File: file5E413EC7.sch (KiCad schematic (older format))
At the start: 4 parts

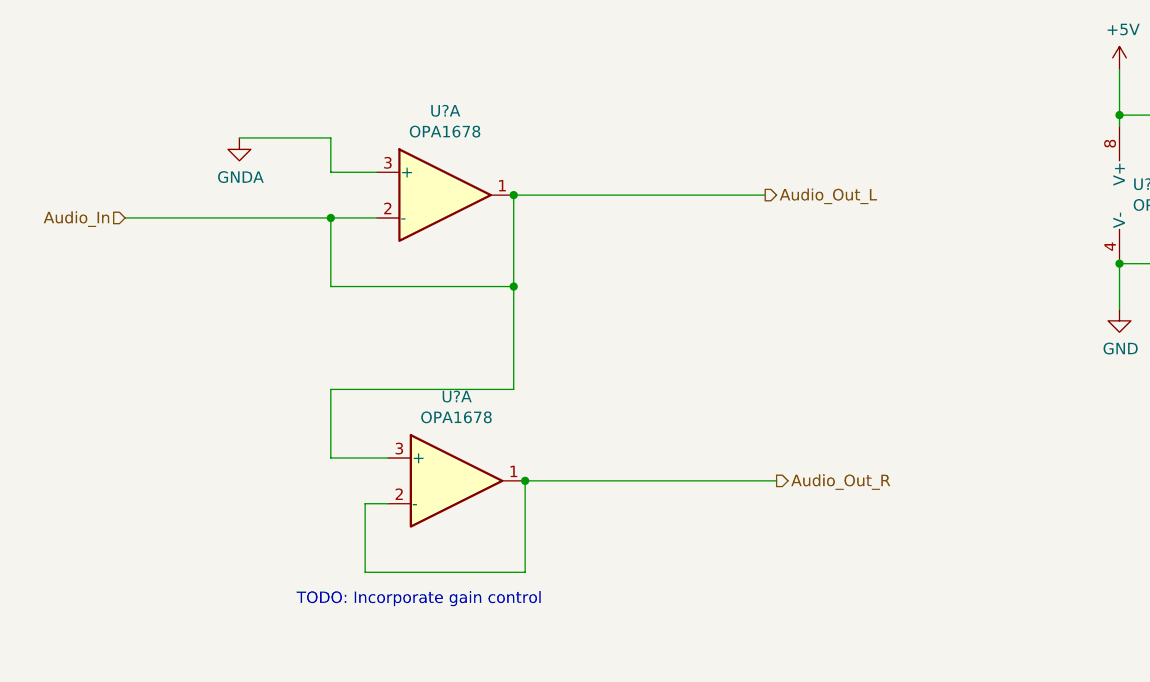
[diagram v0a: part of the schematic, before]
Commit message: Filter calculations, gain stage, oscillation protection
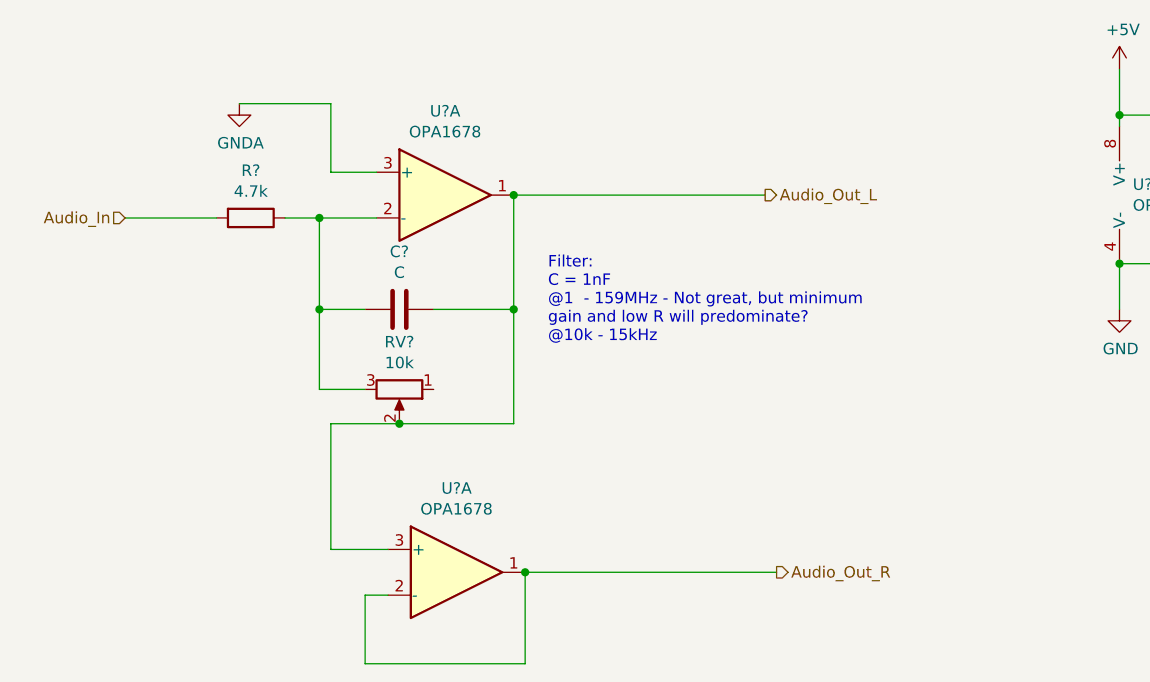
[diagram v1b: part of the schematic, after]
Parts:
- added C?: C, symbol Device:C
- added R?: 4.7k, symbol Device:R
- added RV?: 10k, symbol Device:R_POT
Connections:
- net Audio_In: now also R?.2; no longer U?.1, U?.2 (-), U?.3 (+)
- new net: C?.2, R?.1, RV?.3, U?.2 (-)
- new net Audio_Out_L: C?.1, RV?.2, U?.1, U?.3 (+)
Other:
- note added: "Filter:\nC = 1nF\n@1 - 159MHz - Not great, but minimum \ngain and low R will predominate?\n@10k - 15kHz"
- note removed: "TODO: Incorporate gain control"
- moved on the sheet: U?A
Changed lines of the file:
@@
+	1    0    0    -1
+$EndComp
+$Comp
+L power:GNDA #PWR?
+U 1 1 5E49554A
+P 3750 2200
+F 0 "#PWR?" H 3750 1950 50  0001 C CNN
+F 1 "GNDA" H 3755 2027 50  0000 C CNN
+F 2 "" H 3750 2200 50  0001 C CNN
+F 3 "" H 3750 2200 50  0001 C CNN
+	1    3750 2200
 	1    0    0    -1
 $EndComp
 Wire Wire Line
-	3250 2700 4150 2700
-$Comp
-L power:GNDA #PWR?
-U 1 1 5E49554A
-P 3750 2350
-F 0 "#PWR?" H 3750 2100 50  0001 C CNN
-F 1 "GNDA" H 3755 2177 50  0000 C CNN
-F 2 "" H 3750 2350 50  0001 C CNN
-F 3 "" H 3750 2350 50  0001 C CNN
-	1    3750 2350
-	1    0    0    -1
-$EndComp
+	3750 2200 4150 2200
 Wire Wire Line
-	3750 2350 4150 2350
-Wire Wire Line
-	4150 2350 4150 2500
+	4150 2200 4150 2500
 Wire Wire Line
 	4150 2500 4350 2500
 Wire Wire Line
-	4950 2600 4950 3000
-Wire Wire Line
-	4950 3000 4150 3000
-Wire Wire Line
-	4150 3000 4150 2700
-Connection ~ 4150 2700
-Wire Wire Line
-	4150 2700 4350 2700
-Wire Wire Line
 	6050 2600 4950 2600
 Connection ~ 4950 2600
-Text Notes 4000 4400 0    50   ~ 0
-TODO: Incorporate gain control
 $Comp
 L Amplifier_Operational:OPA1678 U?
@@
 L Amplifier_Operational:OPA1678 U?
 U 1 1 5E49AA78
-P 4700 3850
-F 0 "U?" H 4700 4217 50  0000 C CNN
-F 1 "OPA1678" H 4700 4126 50  0000 C CNN
-F 2 "" H 4700 3850 50  0001 C CNN
-F 3 "http://www.ti.com/lit/ds/symlink/opa1678.pdf" H 4700 3850 50  0001 C CNN
-	1    4700 3850
+P 4700 4250
+F 0 "U?" H 4700 4617 50  0000 C CNN
+F 1 "OPA1678" H 4700 4526 50  0000 C CNN
+F 2 "" H 4700 4250 50  0001 C CNN
+F 3 "http://www.ti.com/lit/ds/symlink/opa1678.pdf" H 4700 4250 50  0001 C CNN
+	1    4700 4250
 	1    0    0    -1
 $EndComp
 Wire Wire Line
-	4950 3000 4950 3450
+	4150 4150 4400 4150
 Wire Wire Line
-	4950 3450 4150 3450
+	5000 4250 5000 4650
 Wire Wire Line
-	4150 3450 4150 3750
+	5000 4650 4300 4650
 Wire Wire Line
-	4150 3750 4400 3750
-Connection ~ 4950 3000
+	4300 4650 4300 4350
 Wire Wire Line
-	5000 3850 5000 4250
-Wire Wire Line
-	5000 4250 4300 4250
-Wire Wire Line
-	4300 4250 4300 3950
-Wire Wire Line
-	4300 3950 4400 3950
-Text HLabel 6100 3850 2    50   Output ~ 0
+	4300 4350 4400 4350
+Text HLabel 6100 4250 2    50   Output ~ 0
 Audio_Out_R
 Wire Wire Line
-	5000 3850 6100 3850
-Connection ~ 5000 3850
+	5000 4250 6100 4250
+Connection ~ 5000 4250
+Wire Wire Line
+	4950 2600 4950 3100
+$Comp
+L Device:R R?
+U 1 1 5E4C4511
+P 3800 2700
+F 0 "R?" V 3593 2700 50  0000 C CNN
+F 1 "4.7k" V 3684 2700 50  0000 C CNN
+F 2 "" V 3730 2700 50  0001 C CNN
+F 3 "~" H 3800 2700 50  0001 C CNN
+	1    3800 2700
+	0    1    1    0
+$EndComp
+$Comp
+L Device:R_POT RV?
+U 1 1 5E4C4B5E
+P 4450 3450
+F 0 "RV?" V 4243 3450 50  0000 C CNN
+F 1 "10k" V 4334 3450 50  0000 C CNN
+F 2 "" H 4450 3450 50  0001 C CNN
+F 3 "~" H 4450 3450 50  0001 C CNN
+	1    4450 3450
+	0    1    1    0
+$EndComp
+Wire Wire Line
+	4100 2700 4350 2700
+Wire Wire Line
+	4100 2700 3950 2700
+Connection ~ 4100 2700
+Wire Wire Line
+	3650 2700 3250 2700
+$Comp
+L Device:C C?
+U 1 1 5E4D4CD0
+P 4450 3100
+F 0 "C?" V 4198 3100 50  0000 C CNN
+F 1 "C" V 4289 3100 50  0000 C CNN
+F 2 "" H 4488 2950 50  0001 C CNN
+F 3 "~" H 4450 3100 50  0001 C CNN
+	1    4450 3100
+	0    1    1    0
+$EndComp
+Wire Wire Line
+	4300 3450 4100 3450
+Wire Wire Line
+	4100 2700 4100 3100
+Wire Wire Line
+	4600 3100 4950 3100
+Connection ~ 4950 3100
+Wire Wire Line
+	4300 3100 4100 3100
+Connection ~ 4100 3100
+Wire Wire Line
+	4100 3100 4100 3450
+Wire Wire Line
+	4450 3600 4950 3600
+Wire Wire Line
+	4950 3100 4950 3600
+Connection ~ 4450 3600
+Wire Wire Line
+	4450 3600 4150 3600
+Wire Wire Line
+	4150 3600 4150 4150
+Text Notes 5100 3250 0    50   ~ 0
+Filter:\nC = 1nF\n@1  - 159MHz - Not great, but minimum \ngain and low R will predominate?\n@10k - 15kHz
 $EndSCHEMATC

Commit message: WIP
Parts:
- C?: value C -> 1nF
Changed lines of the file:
@@
 P 4450 3100
 F 0 "C?" V 4198 3100 50  0000 C CNN
-F 1 "C" V 4289 3100 50  0000 C CNN
+F 1 "1nF" V 4289 3100 50  0000 C CNN
 F 2 "" H 4488 2950 50  0001 C CNN
 F 3 "~" H 4450 3100 50  0001 C CNN

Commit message: Ferrite beads and annotations
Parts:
- gave numbers to parts that had none: 6
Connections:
- no-connect marks 0 -> 1
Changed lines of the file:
@@
 Audio_Out_L
 $Comp
-L Amplifier_Operational:OPA1678 U?
+L Amplifier_Operational:OPA1678 U5
 U 1 1 5E491E4B
 P 4650 2600
-F 0 "U?" H 4650 2967 50  0000 C CNN
+F 0 "U5" H 4650 2967 50  0000 C CNN
 F 1 "OPA1678" H 4650 2876 50  0000 C CNN
 F 2 "" H 4650 2600 50  0001 C CNN
@@
 $EndComp
 $Comp
-L power:GNDA #PWR?
+L power:GNDA #PWR035
 U 1 1 5E49554A
 P 3750 2200
-F 0 "#PWR?" H 3750 1950 50  0001 C CNN
+F 0 "#PWR035" H 3750 1950 50  0001 C CNN
 F 1 "GNDA" H 3755 2027 50  0000 C CNN
 F 2 "" H 3750 2200 50  0001 C CNN
@@
 Connection ~ 4950 2600
 $Comp
-L Amplifier_Operational:OPA1678 U?
+L Amplifier_Operational:OPA1678 U5
 U 3 1 5E497090
 P 7700 2600
-F 0 "U?" H 7658 2646 50  0000 L CNN
+F 0 "U5" H 7658 2646 50  0000 L CNN
 F 1 "OPA1678" H 7658 2555 50  0000 L CNN
 F 2 "" H 7700 2600 50  0001 C CNN
@@
 $EndComp
 $Comp
-L power:+5V #PWR?
+L power:+5V #PWR034
 U 1 1 5E4984E8
 P 7600 2050
-F 0 "#PWR?" H 7600 1900 50  0001 C CNN
+F 0 "#PWR034" H 7600 1900 50  0001 C CNN
 F 1 "+5V" H 7615 2223 50  0000 C CNN
 F 2 "" H 7600 2050 50  0001 C CNN
@@
 $EndComp
 $Comp
-L power:GND #PWR?
+L power:GND #PWR036
 U 1 1 5E4987EF
 P 7600 3100
-F 0 "#PWR?" H 7600 2850 50  0001 C CNN
+F 0 "#PWR036" H 7600 2850 50  0001 C CNN
 F 1 "GND" H 7605 2927 50  0000 C CNN
 F 2 "" H 7600 3100 50  0001 C CNN
@@
 	7600 2300 7600 2250
 $Comp
-L Device:C C?
+L Device:C C12
 U 1 1 5E49915D
 P 8250 2550
-F 0 "C?" H 8365 2596 50  0000 L CNN
+F 0 "C12" H 8365 2596 50  0000 L CNN
 F 1 "0.1uF" H 8365 2505 50  0000 L CNN
 F 2 "" H 8288 2400 50  0001 C CNN
@@
 Connection ~ 7600 2900
 $Comp
-L Amplifier_Operational:OPA1678 U?
+L Amplifier_Operational:OPA1678 U6
 U 1 1 5E49AA78
 P 4700 4250
-F 0 "U?" H 4700 4617 50  0000 C CNN
+F 0 "U6" H 4700 4617 50  0000 C CNN
 F 1 "OPA1678" H 4700 4526 50  0000 C CNN
 F 2 "" H 4700 4250 50  0001 C CNN
@@
 	4950 2600 4950 3100
 $Comp
-L Device:R R?
+L Device:R R9
 U 1 1 5E4C4511
 P 3800 2700
-F 0 "R?" V 3593 2700 50  0000 C CNN
+F 0 "R9" V 3593 2700 50  0000 C CNN
 F 1 "4.7k" V 3684 2700 50  0000 C CNN
 F 2 "" V 3730 2700 50  0001 C CNN
@@
 $EndComp
 $Comp
-L Device:R_POT RV?
+L Device:R_POT RV4
 U 1 1 5E4C4B5E
 P 4450 3450
-F 0 "RV?" V 4243 3450 50  0000 C CNN
+F 0 "RV4" V 4243 3450 50  0000 C CNN
 F 1 "10k" V 4334 3450 50  0000 C CNN
 F 2 "" H 4450 3450 50  0001 C CNN
@@
 	3650 2700 3250 2700
 $Comp
-L Device:C C?
+L Device:C C13
 U 1 1 5E4D4CD0
 P 4450 3100
-F 0 "C?" V 4198 3100 50  0000 C CNN
+F 0 "C13" V 4198 3100 50  0000 C CNN
 F 1 "1nF" V 4289 3100 50  0000 C CNN
 F 2 "" H 4488 2950 50  0001 C CNN
@@
 Text Notes 5100 3250 0    50   ~ 0
 Filter:\nC = 1nF\n@1  - 159MHz - Not great, but minimum \ngain and low R will predominate?\n@10k - 15kHz
+NoConn ~ 4600 3450
 $EndSCHEMATC

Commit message: Layout, 2020-05 order
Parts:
- C12, C13: footprint (none) -> Capacitors_SMD:C_0805_HandSoldering
- R9: footprint (none) -> Resistors_SMD:R_0805_HandSoldering
- RV4: footprint (none) -> BVH_Components_Misc:Potentiometer_TT_P090S-Top-Adjust
- U5: footprint (none) -> SMD_Packages:SOIC-8-N
- U5: renamed from U6; footprint (none) -> SMD_Packages:SOIC-8-N
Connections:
- net Audio_Out_L: now also U5.5 (+); no longer U5.3 (+)
- net Audio_Out_R: now also U5.6 (-), U5.7; no longer U5.1, U5.2 (-)
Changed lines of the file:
@@
 F 0 "U5" H 4650 2967 50  0000 C CNN
 F 1 "OPA1678" H 4650 2876 50  0000 C CNN
-F 2 "" H 4650 2600 50  0001 C CNN
+F 2 "SMD_Packages:SOIC-8-N" H 4650 2600 50  0001 C CNN
 F 3 "http://www.ti.com/lit/ds/symlink/opa1678.pdf" H 4650 2600 50  0001 C CNN
 	1    4650 2600
@@
 F 0 "U5" H 7658 2646 50  0000 L CNN
 F 1 "OPA1678" H 7658 2555 50  0000 L CNN
-F 2 "" H 7700 2600 50  0001 C CNN
+F 2 "SMD_Packages:SOIC-8-N" H 7700 2600 50  0001 C CNN
 F 3 "http://www.ti.com/lit/ds/symlink/opa1678.pdf" H 7700 2600 50  0001 C CNN
 	3    7700 2600
@@
 F 0 "C12" H 8365 2596 50  0000 L CNN
 F 1 "0.1uF" H 8365 2505 50  0000 L CNN
-F 2 "" H 8288 2400 50  0001 C CNN
+F 2 "Capacitors_SMD:C_0805_HandSoldering" H 8288 2400 50  0001 C CNN
 F 3 "~" H 8250 2550 50  0001 C CNN
 	1    8250 2550
@@
 Connection ~ 7600 2900
 $Comp
-L Amplifier_Operational:OPA1678 U6
-U 1 1 5E49AA78
+L Amplifier_Operational:OPA1678 U5
+U 2 1 5E49AA78
 P 4700 4250
-F 0 "U6" H 4700 4617 50  0000 C CNN
+F 0 "U5" H 4700 4617 50  0000 C CNN
 F 1 "OPA1678" H 4700 4526 50  0000 C CNN
-F 2 "" H 4700 4250 50  0001 C CNN
+F 2 "SMD_Packages:SOIC-8-N" H 4700 4250 50  0001 C CNN
 F 3 "http://www.ti.com/lit/ds/symlink/opa1678.pdf" H 4700 4250 50  0001 C CNN
-	1    4700 4250
+	2    4700 4250
 	1    0    0    -1
 $EndComp
@@
 F 0 "R9" V 3593 2700 50  0000 C CNN
 F 1 "4.7k" V 3684 2700 50  0000 C CNN
-F 2 "" V 3730 2700 50  0001 C CNN
+F 2 "Resistors_SMD:R_0805_HandSoldering" V 3730 2700 50  0001 C CNN
 F 3 "~" H 3800 2700 50  0001 C CNN
 	1    3800 2700
@@
 F 0 "RV4" V 4243 3450 50  0000 C CNN
 F 1 "10k" V 4334 3450 50  0000 C CNN
-F 2 "" H 4450 3450 50  0001 C CNN
+F 2 "BVH_Components_Misc:Potentiometer_TT_P090S-Top-Adjust" H 4450 3450 50  0001 C CNN
 F 3 "~" H 4450 3450 50  0001 C CNN
 	1    4450 3450
@@
 F 0 "C13" V 4198 3100 50  0000 C CNN
 F 1 "1nF" V 4289 3100 50  0000 C CNN
-F 2 "" H 4488 2950 50  0001 C CNN
+F 2 "Capacitors_SMD:C_0805_HandSoldering" H 4488 2950 50  0001 C CNN
 F 3 "~" H 4450 3100 50  0001 C CNN
 	1    4450 3100

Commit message: Backup
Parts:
- added V1, V2, V3, V4: VSOURCE, symbol pspice:VSOURCE
- U5: Spice_Lib_File (none) -> /home/benvh/projects/kicad-library/Simulation/OPA1678/OPA16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; Spice_Model (none) -> OPA1678-dual; Spice_Netlist_Enabled (none) -> Y; Spice_Primitive (none) -> X
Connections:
- net Audio_Out_L is gone; now on net GND: C13.1, RV4.2, U5.1, U5.5 (+)
- net Audio_Out_R is gone; now on net GND: U5.6 (-), U5.7
- net +5V: now also V2.1 (E1), V3.1 (E1)
- net Audio_In: now also V1.1 (E1)
- net GND: now also V2.2 (E2), V4.2 (E2)
- net GNDA: now also V1.2 (E2), V3.2 (E2), V4.1 (E1)
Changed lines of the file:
@@
 F 2 "SMD_Packages:SOIC-8-N" H 4650 2600 50  0001 C CNN
 F 3 "http://www.ti.com/lit/ds/symlink/opa1678.pdf" H 4650 2600 50  0001 C CNN
+F 4 "X" H 4650 2600 50  0001 C CNN "Spice_Primitive"
+F 5 "OPA1678-dual" H 4650 2600 50  0001 C CNN "Spice_Model"
+F 6 "Y" H 4650 2600 50  0001 C CNN "Spice_Netlist_Enabled"
+F 7 "/home/benvh/projects/kicad-library/Simulation/OPA1678/OPA1678-dual.lib" H 4650 2600 50  0001 C CNN "Spice_Lib_File"
 	1    4650 2600
 	1    0    0    -1
@@
 F 2 "SMD_Packages:SOIC-8-N" H 7700 2600 50  0001 C CNN
 F 3 "http://www.ti.com/lit/ds/symlink/opa1678.pdf" H 7700 2600 50  0001 C CNN
+F 4 "X" H 7700 2600 50  0001 C CNN "Spice_Primitive"
+F 5 "OPA1678-dual" H 7700 2600 50  0001 C CNN "Spice_Model"
+F 6 "Y" H 7700 2600 50  0001 C CNN "Spice_Netlist_Enabled"
+F 7 "/home/benvh/projects/kicad-library/Simulation/OPA1678/OPA1678-dual.lib" H 7700 2600 50  0001 C CNN "Spice_Lib_File"
 	3    7700 2600
 	1    0    0    -1
@@
 F 2 "SMD_Packages:SOIC-8-N" H 4700 4250 50  0001 C CNN
 F 3 "http://www.ti.com/lit/ds/symlink/opa1678.pdf" H 4700 4250 50  0001 C CNN
+F 4 "X" H 4700 4250 50  0001 C CNN "Spice_Primitive"
+F 5 "OPA1678-dual" H 4700 4250 50  0001 C CNN "Spice_Model"
+F 6 "Y" H 4700 4250 50  0001 C CNN "Spice_Netlist_Enabled"
+F 7 "/home/benvh/projects/kicad-library/Simulation/OPA1678/OPA1678-dual.lib" H 4700 4250 50  0001 C CNN "Spice_Lib_File"
 	2    4700 4250
 	1    0    0    -1
@@
 Filter:\nC = 1nF\n@1  - 159MHz - Not great, but minimum \ngain and low R will predominate?\n@10k - 15kHz
 NoConn ~ 4600 3450
+$Comp
+L pspice:VSOURCE V1
+U 1 1 5EE73326
+P 2050 3350
+F 0 "V1" H 2278 3396 50  0000 L CNN
+F 1 "VSOURCE" H 2278 3305 50  0000 L CNN
+F 2 "" H 2050 3350 50  0001 C CNN
+F 3 "~" H 2050 3350 50  0001 C CNN
+F 4 "V" H 2050 3350 50  0001 C CNN "Spice_Primitive"
+F 5 "dc 0 ac 1" H 2050 3350 50  0001 C CNN "Spice_Model"
+F 6 "Y" H 2050 3350 50  0001 C CNN "Spice_Netlist_Enabled"
+	1    2050 3350
+	1    0    0    -1
+$EndComp
+Text HLabel 2000 2800 0    50   Input ~ 0
+Audio_In
+Wire Wire Line
+	2050 3050 2050 2800
+Wire Wire Line
+	2050 2800 2000 2800
+$Comp
+L pspice:VSOURCE V2
+U 1 1 5EE76558
+P 2000 5200
+F 0 "V2" H 2228 5246 50  0000 L CNN
+F 1 "VSOURCE" H 2228 5155 50  0000 L CNN
+F 2 "" H 2000 5200 50  0001 C CNN
+F 3 "~" H 2000 5200 50  0001 C CNN
+F 4 "V" H 2000 5200 50  0001 C CNN "Spice_Primitive"
+F 5 "dc 5 ac 0" H 2000 5200 50  0001 C CNN "Spice_Model"
+F 6 "Y" H 2000 5200 50  0001 C CNN "Spice_Netlist_Enabled"
+	1    2000 5200
+	1    0    0    -1
+$EndComp
+$Comp
+L power:+5V #PWR037
+U 1 1 5EE76C83
+P 2000 4900
+F 0 "#PWR037" H 2000 4750 50  0001 C CNN
+F 1 "+5V" H 2015 5073 50  0000 C CNN
+F 2 "" H 2000 4900 50  0001 C CNN
+F 3 "" H 2000 4900 50  0001 C CNN
+	1    2000 4900
+	1    0    0    -1
+$EndComp
+$Comp
+L power:GND #PWR038
+U 1 1 5EE771E4
+P 2000 5500
+F 0 "#PWR038" H 2000 5250 50  0001 C CNN
+F 1 "GND" H 2005 5327 50  0000 C CNN
+F 2 "" H 2000 5500 50  0001 C CNN
+F 3 "" H 2000 5500 50  0001 C CNN
+	1    2000 5500
+	1    0    0    -1
+$EndComp
+$Comp
+L power:GNDA #PWR040
+U 1 1 5EE7A598
+P 4250 5950
+F 0 "#PWR040" H 4250 5700 50  0001 C CNN
+F 1 "GNDA" H 4255 5777 50  0000 C CNN
+F 2 "" H 4250 5950 50  0001 C CNN
+F 3 "" H 4250 5950 50  0001 C CNN
+	1    4250 5950
+	1    0    0    -1
+$EndComp
+$Comp
+L pspice:VSOURCE V3
+U 1 1 5EE7AAB6
+P 3650 5650
+F 0 "V3" H 3878 5696 50  0000 L CNN
+F 1 "VSOURCE" H 3878 5605 50  0000 L CNN
+F 2 "" H 3650 5650 50  0001 C CNN
+F 3 "~" H 3650 5650 50  0001 C CNN
+F 4 "V" H 3650 5650 50  0001 C CNN "Spice_Primitive"
+F 5 "dc 2.5 ac 0" H 3650 5650 50  0001 C CNN "Spice_Model"
+F 6 "Y" H 3650 5650 50  0001 C CNN "Spice_Netlist_Enabled"
+	1    3650 5650
+	1    0    0    -1
+$EndComp
+$Comp
+L pspice:VSOURCE V4
+U 1 1 5EE7EF7B
+P 3650 6250
+F 0 "V4" H 3878 6296 50  0000 L CNN
+F 1 "VSOURCE" H 3878 6205 50  0000 L CNN
+F 2 "" H 3650 6250 50  0001 C CNN
+F 3 "~" H 3650 6250 50  0001 C CNN
+F 4 "V" H 3650 6250 50  0001 C CNN "Spice_Primitive"
+F 5 "dc 2.5 ac 0" H 3650 6250 50  0001 C CNN "Spice_Model"
+F 6 "Y" H 3650 6250 50  0001 C CNN "Spice_Netlist_Enabled"
+	1    3650 6250
+	1    0    0    -1
+$EndComp
+$Comp
+L power:+5V #PWR039
+U 1 1 5EE8179E
+P 3650 5350
+F 0 "#PWR039" H 3650 5200 50  0001 C CNN
+F 1 "+5V" H 3665 5523 50  0000 C CNN
+F 2 "" H 3650 5350 50  0001 C CNN
+F 3 "" H 3650 5350 50  0001 C CNN
+	1    3650 5350
+	1    0    0    -1
+$EndComp
+$Comp
+L power:GND #PWR041
+U 1 1 5EE81CED
+P 3650 6550
+F 0 "#PWR041" H 3650 6300 50  0001 C CNN
+F 1 "GND" H 3655 6377 50  0000 C CNN
+F 2 "" H 3650 6550 50  0001 C CNN
+F 3 "" H 3650 6550 50  0001 C CNN
+	1    3650 6550
+	1    0    0    -1
+$EndComp
+Wire Wire Line
+	3650 5950 4250 5950
+Connection ~ 3650 5950
+$Comp
+L power:GNDA #PWR01
+U 1 1 5EE87F7A
+P 2050 3650
+F 0 "#PWR01" H 2050 3400 50  0001 C CNN
+F 1 "GNDA" H 2055 3477 50  0000 C CNN
+F 2 "" H 2050 3650 50  0001 C CNN
+F 3 "" H 2050 3650 50  0001 C CNN
+	1    2050 3650
+	1    0    0    -1
+$EndComp
+Text HLabel 8300 4750 2    50   Output ~ 0
+Audio_Out_R
+Text HLabel 8300 4450 2    50   Output ~ 0
+Audio_Out_L
+$Comp
+L power:GND #PWR?
+U 1 1 5EE8F230
+P 7650 4600
+F 0 "#PWR?" H 7650 4350 50  0001 C CNN
+F 1 "GND" H 7655 4427 50  0000 C CNN
+F 2 "" H 7650 4600 50  0001 C CNN
+F 3 "" H 7650 4600 50  0001 C CNN
+	1    7650 4600
+	1    0    0    -1
+$EndComp
+Wire Wire Line
+	7650 4600 7650 4550
+Wire Wire Line
+	7650 4450 8300 4450
+Wire Wire Line
+	7650 4550 8300 4550
+Wire Wire Line
+	8300 4550 8300 4750
+Connection ~ 7650 4550
+Wire Wire Line
+	7650 4550 7650 4450
 $EndSCHEMATC
